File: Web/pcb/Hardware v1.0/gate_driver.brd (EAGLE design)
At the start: 49.2 x 55.9 mm, 25 parts, among them IC1 HCPL3120, IC2 HCPL3120

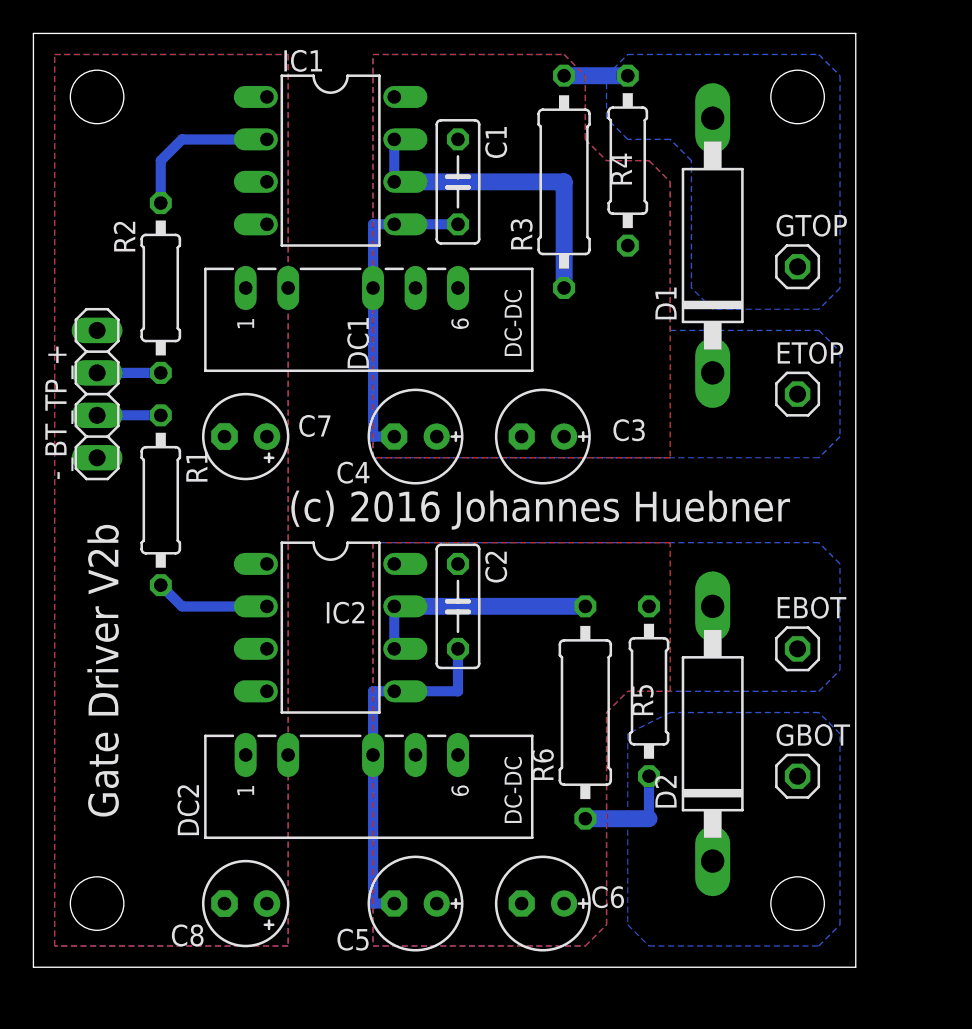
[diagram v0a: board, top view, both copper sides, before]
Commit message: converted updater to php
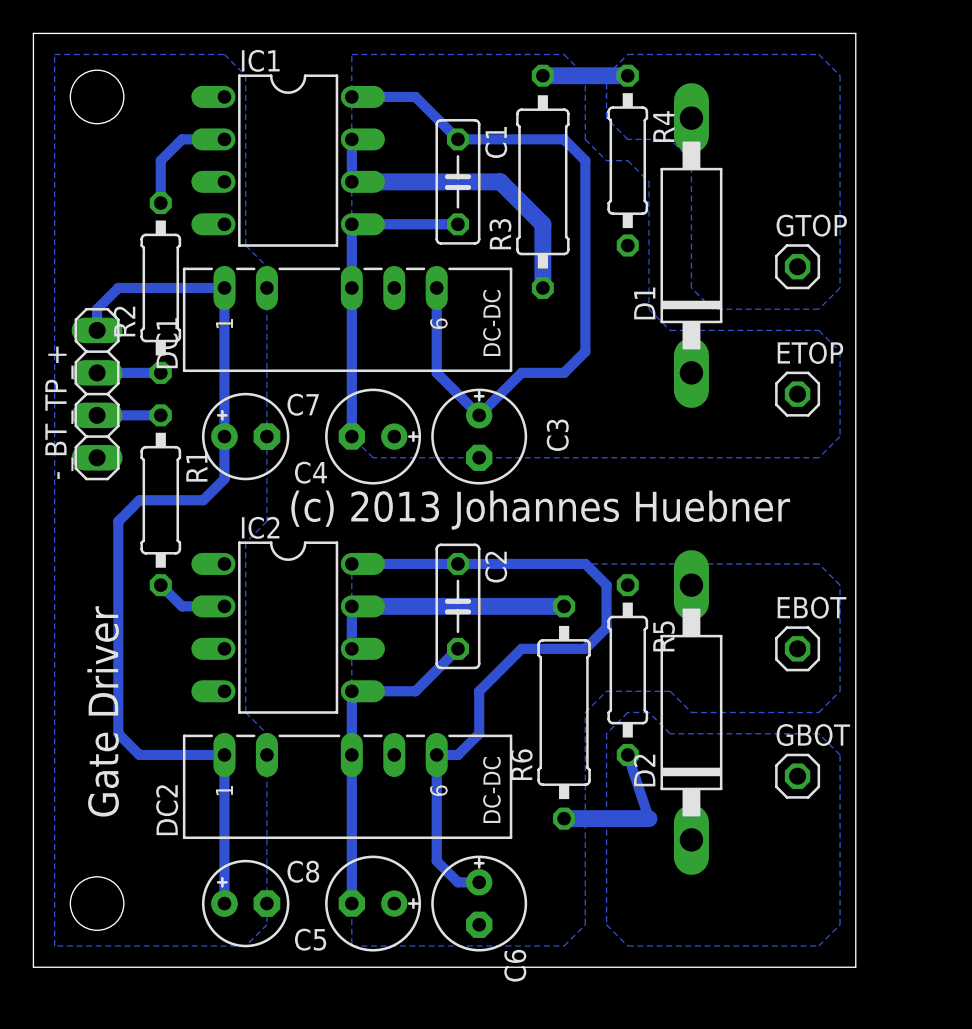
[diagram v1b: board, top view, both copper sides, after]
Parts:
- R3, R6: value 4R7 -> 10R
- moved C3 3.81 mm to (26.7, 31.8), turned to 270 degrees
- moved C6 3.81 mm to (26.7, 3.81), turned to 270 degrees
- moved IC1 2.54 mm to (15.2, 48.3)
- moved IC2 2.54 mm to (15.2, 20.3)
- moved C4 2.54 mm to (20.3, 31.8)
- moved C5 2.54 mm to (20.3, 3.81)
- moved D2 1.80 mm to (39.4, 15.2)
- moved R5 1.80 mm to (35.6, 17.8)
- moved D1 1.27 mm to (39.4, 43.2)
- moved R6 1.27 mm to (31.8, 15.2)
- moved DC1 1.27 mm to (17.8, 40.6)
- moved DC2 1.27 mm to (17.8, 12.7)
- moved R3 1.27 mm to (30.5, 47.0)
- turned C7 to 0 degrees
- turned C8 to 0 degrees
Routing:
- net N$15: track 0.00 -> 56.7 mm
- net N$7: track 0.00 -> 42.5 mm
- net N$6: track 1.27 -> 43.6 mm
- net GBOT: track 6.35 -> 9.10 mm
- net N$2: track 9.42 -> 6.88 mm
- net N$1: track 6.88 -> 4.34 mm
- net N$8: track 21.6 -> 20.1 mm
- net GTOP: track 3.81 -> 5.08 mm
- net N$10: track 14.0 -> 15.2 mm
- removed copper zone on layer 1, net N$15
- removed copper zone on layer 1, net N$6
- removed copper zone on layer 1, net N$7
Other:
- board text added: "(c) 2013 Johannes Huebner"
- board text added: "Gate Driver"
- board text removed: "(c) 2016 Johannes Huebner"
- board text removed: "Gate Driver V2b"
